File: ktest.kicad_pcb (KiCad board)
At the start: 4 copper layers, 23.9 x 21.1 mm, 7 parts, among them J1 Conn_01x03_Pin

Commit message: update fab doc
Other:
- board text added: "Fabrication notes"
- board text added: "Stackup"
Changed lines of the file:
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@@
 	)
 	(paper "A4")
+	(title_block
+		(title "title")
+		(date "2026-10-01")
+		(rev "0.0.2")
+		(comment 1 "c1")
+		(comment 2 "c2")
+		(comment 3 "c3")
+		(comment 4 "c4")
+	)
 	(layers
 		(0 "F.Cu" signal)
@@
 		(49 "User.6" user "AssemblyTop")
 		(51 "User.7" user "AssemblyBottom")
-		(53 "User.8" user)
+		(53 "User.8" user "FabricationNotes")
+		(55 "User.9" user "FabricationDrillMap")
+		(57 "User.10" user)
 	)
 	(setup
@@
 		(capping no)
 		(filling no)
+		(zone_defaults)
 		(pcbplotparams
 			(layerselection 0x00000000_00000000_55555555_5755f5ff)
@@
 		(layer "User.7")
 	)
+	(gr_rect
+		(start 20 40)
+		(end 90 180)
+		(stroke
+			(width 0.1)
+			(type default)
+		)
+		(fill no)
+		(layer "User.8")
+	)
+	(gr_rect
+		(start 180 40)
+		(end 280 120)
+		(stroke
+			(width 0.1)
+			(type default)
+		)
+		(fill no)
+		(layer "User.8")
+	)
 	(gr_line
 		(start 9.906 9.906)
@@
 			(type default)
 		)
-		(layer "User.8")
+		(layer "User.10")
 	)
 	(gr_line
@@
 			(type default)
 		)
-		(layer "User.8")
+		(layer "User.10")
 	)
 	(gr_text "angled top render"
@@
 		)
 	)
+	(gr_text "Fabrication notes\n"
+		(at 21 41 0)
+		(layer "User.8")
+		(effects
+			(font
+				(size 1 1)
+				(thickness 0.15)
+			)
+			(justify left top)
+		)
+	)
+	(gr_text "Stackup"
+		(at 181 41 0)
+		(layer "User.8")
+		(effects
+			(font
+				(size 1 1)
+				(thickness 0.15)
+			)
+			(justify left top)
+		)
+	)
 	(segment
 		(start 106.892 58.819)
@@
 		(members "60365628-61de-4015-826d-ef046bea2621" "ef773150-5c25-4b16-be8e-16da88ff3160")
 	)
+	(group "stackup"
+		(members "1b6f2de8-c4e3-46fd-9d01-4a1a5133a59f" "b3aabfc6-7e51-4132-9677-4e126ebf5b7c")
+	)
 	(embedded_fonts no)

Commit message: adding tables
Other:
- board text added: "drill table"
- board text added: "parts table top"
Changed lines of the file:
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@@
 		(capping no)
 		(filling no)
-		(zone_defaults)
 		(pcbplotparams
 			(layerselection 0x00000000_00000000_55555555_5755f5ff)
@@
 	)
 	(gr_rect
-		(start 140 40)
-		(end 240 140)
+		(start 20 40)
+		(end 80 100)
 		(stroke
 			(width 0.1)
@@
 		)
 		(fill no)
+		(layer "User.6")
+	)
+	(gr_rect
+		(start 20 40)
+		(end 80 100)
+		(stroke
+			(width 0.1)
+			(type default)
+		)
+		(fill no)
+		(layer "User.7")
+	)
+	(gr_rect
+		(start 140 40)
+		(end 240 140)
+		(stroke
+			(width 0.1)
+			(type default)
+		)
+		(fill no)
 		(layer "User.7")
 	)
@@
 		(fill no)
 		(layer "User.8")
+	)
+	(gr_rect
+		(start 20 40)
+		(end 80 140)
+		(stroke
+			(width 0.1)
+			(type default)
+		)
+		(fill no)
+		(layer "User.9")
 	)
 	(gr_line
@@
 		)
 	)
+	(gr_text "parts table top"
+		(at 21 41 0)
+		(layer "User.6")
+		(effects
+			(font
+				(size 1 1)
+				(thickness 0.15)
+			)
+			(justify left top)
+		)
+	)
 	(gr_text "top render"
 		(at 141 41 0)
@@
 		)
 	)
+	(gr_text "parts table top"
+		(at 21 41 0)
+		(layer "User.7")
+		(effects
+			(font
+				(size 1 1)
+				(thickness 0.15)
+			)
+			(justify left top)
+		)
+	)
 	(gr_text "bottom render"
 		(at 141 41 0)
@@
 		)
 	)
+	(gr_text "drill table"
+		(at 21 41 0)
+		(layer "User.9")
+		(effects
+			(font
+				(size 1 1)
+				(thickness 0.15)
+			)
+			(justify left top)
+		)
+	)
 	(segment
 		(start 106.892 58.819)
@@
 		(members "47a33e86-0a7b-4fb2-9f1a-8c1f9bbd8aef" "e0f4d6b7-6642-4f52-86d4-2c7661283d27")
 	)
+	(group "kibot_table_parts_count_top"
+		(members "99b83e7d-9b0c-45c7-92ac-70cc096771d4" "cced759b-c488-4320-a0d3-57876245a831")
+	)
 	(group "kibot_image_blender_top"
 		(members "3748c16f-f86b-4ed3-95e1-1cd301faa602" "54584b5a-66d1-40a4-a952-5988b66ec816")
@@
 		(members "60365628-61de-4015-826d-ef046bea2621" "ef773150-5c25-4b16-be8e-16da88ff3160")
 	)
+	(group "kibot_table_parts_count_bot"
+		(members "1bf57a67-d281-4813-ae12-dc4ab2eed24c" "3f88ce79-dbcf-4751-89d2-f94466b73522")
+	)
 	(group "stackup"
 		(members "1b6f2de8-c4e3-46fd-9d01-4a1a5133a59f" "b3aabfc6-7e51-4132-9677-4e126ebf5b7c")
 	)
+	(group "kibot_table_drillmap"
+		(members "38ae1b75-e986-47af-b107-83ca89a5d73c" "acffd48d-6b1e-4a74-8447-dbce9f99bef7")
+	)
 	(embedded_fonts no)

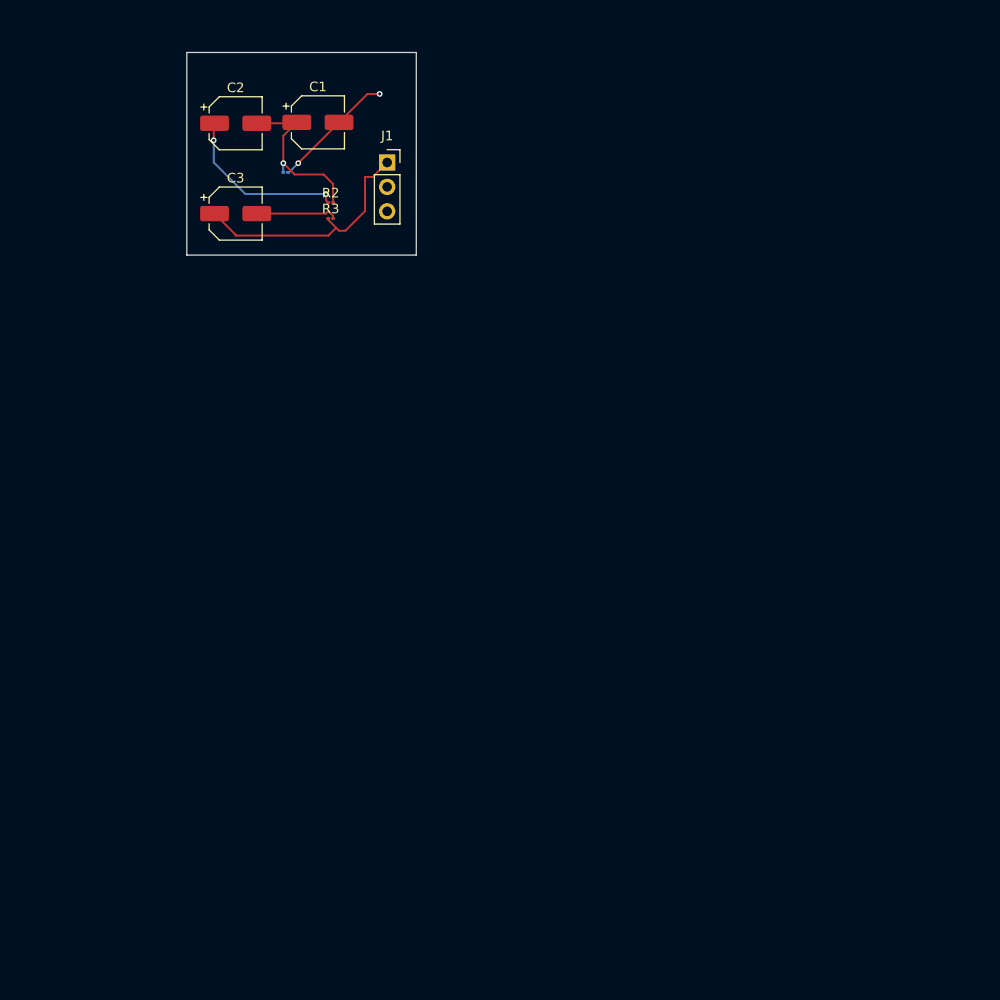
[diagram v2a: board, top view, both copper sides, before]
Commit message: low res render option
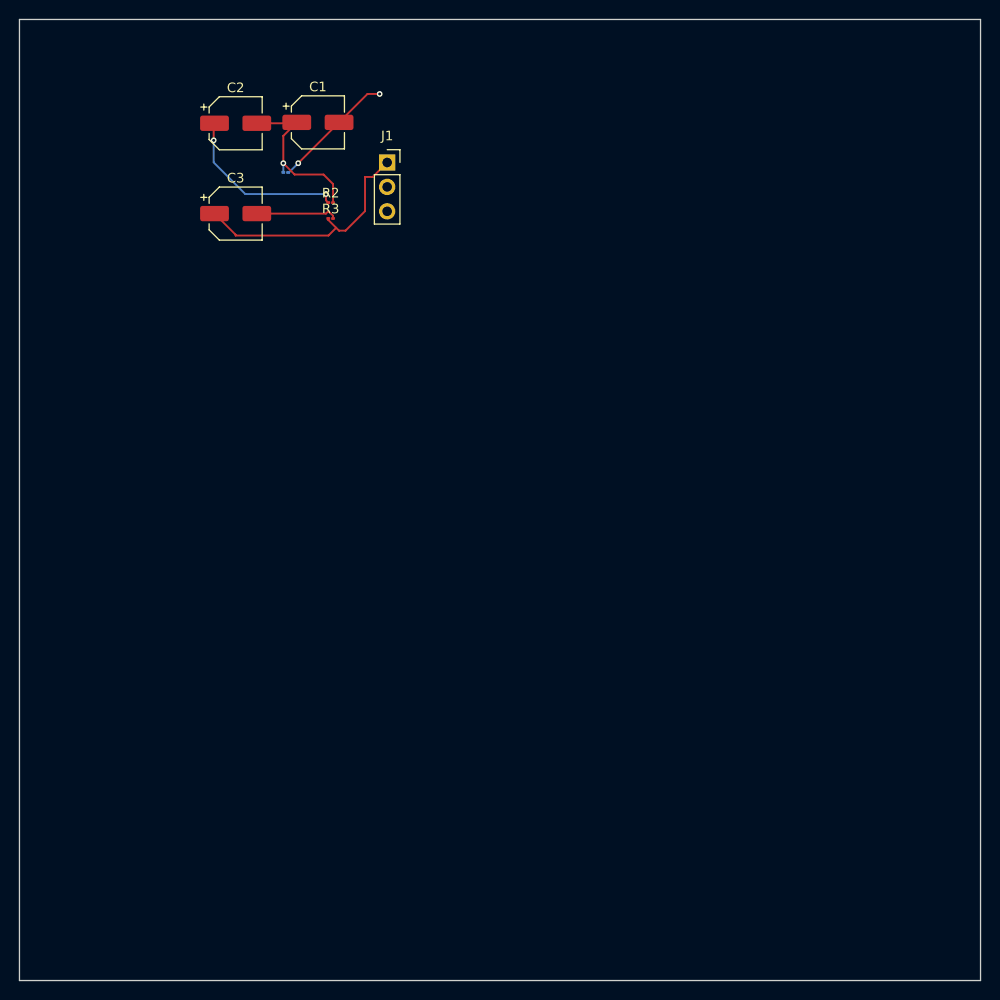
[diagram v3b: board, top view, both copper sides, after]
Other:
- board size 23.9 x 21.1 mm -> 100 x 100 mm
- board text added: "parts table bot"
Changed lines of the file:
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@@
 	)
 	(gr_rect
-		(start 92.414 43.434)
-		(end 116.29 64.516)
+		(start 75 40)
+		(end 175 140)
 		(stroke
 			(width 0.05)
@@
 	(gr_rect
 		(start 20 40)
-		(end 80 100)
+		(end 70 100)
 		(stroke
 			(width 0.1)
@@
 	)
 	(gr_rect
-		(start 140 40)
-		(end 240 140)
+		(start 180 40)
+		(end 280 140)
 		(stroke
 			(width 0.1)
@@
 	(gr_rect
 		(start 20 40)
-		(end 80 100)
+		(end 70 100)
 		(stroke
 			(width 0.1)
@@
 	)
 	(gr_rect
-		(start 140 40)
-		(end 240 140)
+		(start 180 40)
+		(end 280 140)
 		(stroke
 			(width 0.1)
@@
 	)
 	(gr_text "top render"
-		(at 141 41 0)
+		(at 181 41 0)
 		(layer "User.6")
 		(effects
@@
 		)
 	)
-	(gr_text "parts table top"
+	(gr_text "parts table bot"
 		(at 21 41 0)
 		(layer "User.7")
@@
 	)
 	(gr_text "bottom render"
-		(at 141 41 0)
+		(at 181 41 0)
 		(layer "User.7")
 		(effects
@@
 		(members "47a33e86-0a7b-4fb2-9f1a-8c1f9bbd8aef" "e0f4d6b7-6642-4f52-86d4-2c7661283d27")
 	)
+	(group "kibot_image_blender_top"
+		(members "3748c16f-f86b-4ed3-95e1-1cd301faa602" "54584b5a-66d1-40a4-a952-5988b66ec816")
+	)
 	(group "kibot_table_parts_count_top"
 		(members "99b83e7d-9b0c-45c7-92ac-70cc096771d4" "cced759b-c488-4320-a0d3-57876245a831")
 	)
-	(group "kibot_image_blender_top"
-		(members "3748c16f-f86b-4ed3-95e1-1cd301faa602" "54584b5a-66d1-40a4-a952-5988b66ec816")
+	(group "kibot_table_parts_count_bottom"
+		(members "1bf57a67-d281-4813-ae12-dc4ab2eed24c" "3f88ce79-dbcf-4751-89d2-f94466b73522")
 	)
 	(group "kibot_image_blender_bottom"
 		(members "60365628-61de-4015-826d-ef046bea2621" "ef773150-5c25-4b16-be8e-16da88ff3160")
 	)
-	(group "kibot_table_parts_count_bot"
-		(members "1bf57a67-d281-4813-ae12-dc4ab2eed24c" "3f88ce79-dbcf-4751-89d2-f94466b73522")
-	)
 	(group "stackup"
